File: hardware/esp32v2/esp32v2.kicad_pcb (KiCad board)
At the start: 2 copper layers, 22.5 x 29.8 mm, 10 parts, among them J1 Conn_01x01, J2 Conn_01x02, J3 Conn_01x10, J6 Conn_01x01, U2 ESP32-S3-MINI-1-N8

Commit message: wip
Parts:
- removed C18: 10u, Capacitor_SMD:C_0603_1608Metric
- removed C4: 1u, Capacitor_SMD:C_0603_1608Metric
- removed D2, D4: ESD3.3, Package_TO_SOT_SMD:SOT-723
- removed J1, J6: Conn_01x01, Connector_PinHeader_1.00mm:PinHeader_1x01_P1.00mm_Vertical
- removed R2: 10K, Resistor_SMD:R_0402_1005Metric
- removed U2: ESP32-S3-MINI-1-N8, ESP32_S3_MINI_1_N8:XCVR_ESP32-S3-MINI-1-N8
- added AE1: Antenna, RF_Antenna:Texas_SWRA117D_2.4GHz_Left, F.Cu at (119.0, 32.1)
- added BTN1: BTN, Button_Switch_SMD:SW_Push_1P1T_XKB_TS-1187A, F.Cu at (105.6, 37.5)
- added C1: 12pF, Capacitor_SMD:C_0201_0603Metric, F.Cu at (105.4, 48.7)
- added C10: 0.1uF, Capacitor_SMD:C_0201_0603Metric, F.Cu at (107.9, 44.4)
- added C11: 0.1uF, Capacitor_SMD:C_0201_0603Metric, F.Cu at (119.5, 48.6)
- added C13: 1uF, Capacitor_SMD:C_0201_0603Metric, F.Cu at (116.9, 43.0)
- added C15: 0.1uF, Capacitor_SMD:C_0201_0603Metric, F.Cu at (112.8, 54.0)
- added C19: 0.1uF, Capacitor_SMD:C_0201_0603Metric, F.Cu at (110.2, 53.9)
- added C2: 0.1uF, Capacitor_SMD:C_0201_0603Metric, F.Cu at (107.9, 46.6)
- added C25: 10uF, Capacitor_SMD:C_0201_0603Metric, F.Cu at (107.9, 45.9)
- added C26: 1uF, Capacitor_SMD:C_0201_0603Metric, F.Cu at (107.9, 43.7)
- added C31: 15pF, Capacitor_SMD:C_0201_0603Metric, F.Cu at (119.5, 34.0)
- added C32: 0.1uF, Capacitor_SMD:C_0201_0603Metric, F.Cu at (117.1, 42.2)
- added C33: 12pF, Capacitor_SMD:C_0201_0603Metric, F.Cu at (107.5, 51.2)
- added C37: 12pF, Capacitor_SMD:C_0201_0603Metric, F.Cu at (121.1, 45.4)
- added C38: 12pF, Capacitor_SMD:C_0201_0603Metric, F.Cu at (121.1, 46.1)
- added C39: 1uF, Capacitor_SMD:C_0201_0603Metric, F.Cu at (107.9, 45.2)
- added C40: 10nF, Capacitor_SMD:C_0201_0603Metric, F.Cu at (108.6, 51.2)
- added DNP1: 15pF, Capacitor_SMD:C_0201_0603Metric, F.Cu at (110.3, 53.2)
- added Flash1: Flash, Button_Switch_SMD:SW_Push_1P1T_XKB_TS-1187A, F.Cu at (120.6, 39.0)
- added L3: 2nH, Inductor_SMD:L_0201_0603Metric, F.Cu at (119.7, 49.4)
- added L6: 4.7nH, Inductor_SMD:L_0201_0603Metric, F.Cu at (108.8, 52.7)
- added R21: 10K, Resistor_SMD:R_0201_0603Metric, F.Cu at (113.8, 53.0)
- added R22: 10K, Resistor_SMD:R_0201_0603Metric, F.Cu at (111.8, 54.0)
- added R4: 10K, Resistor_SMD:R_0201_0603Metric, F.Cu at (118.3, 49.0)
- added Reset1: Reset, Button_Switch_SMD:SW_Push_1P1T_XKB_TS-1187A, F.Cu at (102.0, 44.4)
- added U1: ESP32-S3, Package_DFN_QFN:QFN-56-1EP_7x7mm_P0.4mm_EP4x4mm, F.Cu at (113.3, 48.1)
- added U3: W25Q128JVS, Package_SO:SOIC-8_5.3x5.3mm_P1.27mm, F.Cu at (113.4, 38.6)
- added Y1: 32.768 kHz, Crystal:Crystal_SMD_3215-2Pin_3.2x1.5mm, F.Cu at (118.8, 45.9)
- added Y2: 40MHz(10ppm), Crystal:Crystal_SMD_2520-4Pin_2.5x2.0mm, F.Cu at (107.4, 48.7)
- moved J2 1.80 mm to (105.5, 56.5)
- moved J3 0.58 mm to (110.0, 56.8)
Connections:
- J2 pad 2: +3V3 -> VDD_CPU
- J3 pad 1: Net-(J3-Pin_1) -> IO1
- J3 pad 10: /USB_D+ -> USB_D+
- J3 pad 2: Net-(J3-Pin_2) -> IO2
- J3 pad 3: Net-(J3-Pin_3) -> IO3
- J3 pad 4: Net-(J3-Pin_4) -> IO4/BAT
- J3 pad 5: Net-(J3-Pin_5) -> IO5
- J3 pad 6: Net-(J3-Pin_6) -> IO6
- J3 pad 7: Net-(J3-Pin_7) -> IO7
- J3 pad 8: Net-(J3-Pin_8) -> IO8
- J3 pad 9: /USB_D- -> USB_D-
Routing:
- net GND: track 92.1 -> 0.00 mm, vias 38 -> 0
- net +3V3: track 44.3 -> 0.00 mm, vias 2 -> 0
- net /ESP32_EN: track 24.7 -> 0.00 mm
- net Net-(J3-Pin_1): track 14.2 -> 0.00 mm
- net /USB_D+: track 11.4 -> 0.00 mm
- net /USB_D-: track 11.1 -> 0.00 mm
- net Net-(J3-Pin_8): track 11.1 -> 0.00 mm
- net Net-(J3-Pin_7): track 11.0 -> 0.00 mm
- net Net-(J3-Pin_6): track 10.9 -> 0.00 mm
- net Net-(J3-Pin_3): track 10.9 -> 0.00 mm
- net Net-(J3-Pin_5): track 10.9 -> 0.00 mm
- net Net-(J3-Pin_4): track 10.8 -> 0.00 mm
- net Net-(J3-Pin_2): track 10.7 -> 0.00 mm
- net /GPIO0: track 5.24 -> 0.00 mm
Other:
- board size 22.5 x 29.8 mm -> 21 x 29.8 mm

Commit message: wip
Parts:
- removed BTN1: BTN, Button_Switch_SMD:SW_Push_1P1T_XKB_TS-1187A
- removed Flash1: Flash, Button_Switch_SMD:SW_Push_1P1T_XKB_TS-1187A
- removed R4: 10K, Resistor_SMD:R_0201_0603Metric
- removed Reset1: Reset, Button_Switch_SMD:SW_Push_1P1T_XKB_TS-1187A
- removed U3: W25Q128JVS, Package_SO:SOIC-8_5.3x5.3mm_P1.27mm
- added C16: 0.1uF, Capacitor_SMD:C_0201_0603Metric, F.Cu at (115.8, 35.3)
- added J1: Conn_01x02, Connector_JST:JST_SH_BM02B-SRSS-TB_1x02-1MP_P1.00mm_Vertical, F.Cu at (106.0, 50.3)
- added R2: 10K, Resistor_SMD:R_0201_0603Metric, F.Cu at (105.5, 47.0)
- moved C15 19.7 mm to (115.5, 34.5), turned to 45 degrees
- moved C37 18.2 mm to (105.6, 36.0)
- moved DNP1 17.9 mm to (117.3, 36.7), turned to 45 degrees
- moved L6 17.8 mm to (118.0, 37.5), turned to 45 degrees
- moved Y1 16.4 mm to (107.0, 34.5), turned to 180 degrees
- moved C38 15.9 mm to (109.8, 35.0)
- moved C1 15.1 mm to (118.2, 40.8), turned to 45 degrees
- moved C33 13.2 mm to (117.0, 42.0), turned to 45 degrees
- moved C19 12.9 mm to (117.0, 43.0), turned to 45 degrees
- moved J2 12.5 mm to (115.5, 49.0)
- moved C11 11.1 mm to (108.8, 45.3)
- moved C13 10.9 mm to (106.2, 40.7), turned to 135 degrees
- moved C32 10.3 mm to (107.0, 40.5), turned to 135 degrees
- moved C40 8.93 mm to (114.3, 44.2), turned to -135 degrees
- moved R22 8.79 mm to (106.5, 47.0), turned to 90 degrees
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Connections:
- J2 pad 1: GND -> VDD_CPU
- J2 pad 2: VDD_CPU -> GND
- J3 pad 1: IO1 -> USB_D-
- J3 pad 10: USB_D+ -> IO1
- J3 pad 2: IO2 -> USB_D+
- J3 pad 3: IO3 -> IO8
- J3 pad 4: IO4/BAT -> IO7
- J3 pad 5: IO5 -> IO6
- J3 pad 6: IO6 -> IO5
- J3 pad 7: IO7 -> IO4/BAT
- J3 pad 8: IO8 -> IO3
- J3 pad 9: USB_D- -> IO2
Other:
- board size 21 x 29.8 mm -> 18 x 37.5 mm

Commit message: wip
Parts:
- removed C37, C38: 12pF, Capacitor_SMD:C_0201_0603Metric
- removed Y1: 32.768 kHz, Crystal:Crystal_SMD_3215-2Pin_3.2x1.5mm
- moved C32 12.8 mm to (114.8, 50.7), turned to 45 degrees
- moved C13 12.1 mm to (114.0, 50.0), turned to 45 degrees
- moved J1 11.9 mm to (105.2, 38.5), turned to 90 degrees
- moved C31 11.1 mm to (109.2, 38.2), turned to 135 degrees
- moved J2 11.1 mm to (105.0, 52.5)
- moved Y2 10.8 mm to (116.1, 40.6), turned to -45 degrees
- moved C15 9.91 mm to (108.2, 41.2), turned to 135 degrees
- moved C16 8.92 mm to (108.8, 40.8), turned to 135 degrees
- moved C19 8.23 mm to (109.2, 40.2), turned to 135 degrees
- moved L6 7.96 mm to (110.2, 39.2), turned to 135 degrees
- moved J3 7.62 mm to (109.5, 53.8)
- moved DNP1 6.85 mm to (110.7, 38.7), turned to 135 degrees
- moved L3 6.53 mm to (109.7, 39.7), turned to -45 degrees
- moved U1 6.15 mm to (111.4, 45.4), turned to -45 degrees
- moved R22 5.38 mm to (107.7, 41.7), turned to 135 degrees
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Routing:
- net IO1: track 0.00 -> 16.0 mm, vias 0 -> 2
- net IO2: track 0.00 -> 15.1 mm, vias 0 -> 2
- net IO3: track 0.00 -> 14.3 mm, vias 0 -> 2
- net IO4/BAT: track 0.00 -> 13.6 mm, vias 0 -> 2
- net EN: track 0.00 -> 13.4 mm, vias 0 -> 2
- net IO5: track 0.00 -> 13.0 mm, vias 0 -> 2
- net IO6: track 0.00 -> 12.4 mm, vias 0 -> 2
- net IO7: track 0.00 -> 11.8 mm, vias 0 -> 2
- net IO0: track 0.00 -> 11.7 mm
- net IO8: track 0.00 -> 11.2 mm, vias 0 -> 2
- net GND: track 0.00 -> 9.86 mm
- net VDD_CPU: track 0.00 -> 9.32 mm
- net Net-(U1-XTAL_N): track 0.00 -> 6.69 mm
- net USB_D+: track 0.00 -> 5.81 mm
- net USB_D-: track 0.00 -> 5.28 mm
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- removed copper zone on B.Cu, net GND
- removed copper zone on F.Cu, net GND
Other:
- board size 18 x 37.5 mm -> 20 x 25.5 mm
- copper layers 2 -> 4

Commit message: wip esp32 v2
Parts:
- removed AE1: Antenna, RF_Antenna:Texas_SWRA117D_2.4GHz_Left
- moved C32 1.60 mm to (113.2, 51.3)
- moved C13 1.47 mm to (112.7, 50.8)
- moved C16 0.71 mm to (108.3, 40.3)
- moved J1 0.20 mm to (105.2, 38.3)
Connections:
- J3 pad 10: IO1 -> IO38
- J3 pad 3: IO8 -> IO48
- J3 pad 4: IO7 -> IO47
- J3 pad 5: IO6 -> IO33
- J3 pad 6: IO5 -> IO34
- J3 pad 7: IO4/BAT -> IO35
- J3 pad 8: IO3 -> IO36
- J3 pad 9: IO2 -> IO37
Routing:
- net VDD_CPU: track 9.32 -> 25.8 mm, vias 0 -> 6
- net IO1: track 16.0 -> 0.00 mm, vias 2 -> 0
- net IO2: track 15.1 -> 0.00 mm, vias 2 -> 0
- net IO3: track 14.3 -> 0.00 mm, vias 2 -> 0
- net IO4/BAT: track 13.6 -> 0.00 mm, vias 2 -> 0
- net IO5: track 13.0 -> 0.09 mm, vias 2 -> 0
- net IO6: track 12.4 -> 0.00 mm, vias 2 -> 0
- net IO7: track 11.8 -> 0.00 mm, vias 2 -> 0
- net IO8: track 11.2 -> 0.00 mm, vias 2 -> 0
- net GND: track 9.86 -> 20.8 mm, vias 0 -> 9
- net IO38: track 0.00 -> 10.4 mm
- net IO37: track 0.00 -> 8.82 mm
- net IO36: track 0.00 -> 8.24 mm
- net IO35: track 0.00 -> 7.66 mm
- net IO34: track 0.00 -> 7.08 mm
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- added copper zone on B.Cu, net GND
- added copper zone on In1.Cu, net VDD_CPU

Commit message: wip
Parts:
- removed J3: Conn_01x10, LIB_SM10B-SRSS-TB_LF__SN_:SM10B-SRSS-TB
- added J4: Conn_01x02, Connector_Coaxial:U.FL_Molex_MCRF_73412-0110_Vertical, F.Cu at (118.5, 40.5)
- added J5: Conn_01x02, Connector_JST:JST_SH_BM02B-SRSS-TB_1x02-1MP_P1.00mm_Vertical, F.Cu at (105.2, 53.3)
- added S1: Tactile Button, 160gf, PCM_JLCPCB:SW_TS-1088-AR02016, F.Cu at (106.2, 42.5)
- added S2: Tactile Button, 160gf, PCM_JLCPCB:SW_TS-1088-AR02016, F.Cu at (106.3, 39.0)
- C31: value 15pF -> 4pF
- DNP1: value 15pF -> 5pF
- J1: value Conn_01x02 -> Conn_01x08; footprint Connector_JST:JST_SH_BM02B-SRSS-TB_1x02-1MP_P1.00mm_Vertical -> Connector_JST:JST_SHL_SM08B-SHLS-TF_1x08-1MP_P1.00mm_Horizontal
- L6: value 4.7nH -> 1.8nH
- moved J1 23.9 mm to (115.0, 60.0), turned to 0 degrees
- moved C31 10.1 mm to (117.5, 44.0), turned to 0 degrees
- moved Y2 9.30 mm to (119.3, 49.3), turned to -90 degrees
- moved C33 9.27 mm to (119.0, 51.7), turned to 0 degrees
- moved C1 9.13 mm to (119.0, 47.0), turned to 0 degrees
- moved DNP1 8.98 mm to (117.4, 44.7), turned to 0 degrees
- moved C40 7.90 mm to (117.2, 46.4), turned to 90 degrees
- moved L6 7.72 mm to (116.1, 44.2), turned to 90 degrees
- moved L3 7.24 mm to (115.4, 44.2), turned to -90 degrees
- moved C19 6.77 mm to (114.7, 44.2), turned to 90 degrees
- moved J2 6.40 mm to (105.0, 58.9)
- moved C16 6.26 mm to (113.5, 43.7), turned to 180 degrees
- moved C15 6.12 mm to (113.5, 44.4), turned to 180 degrees
- moved R2 5.91 mm to (113.2, 42.3), turned to 0 degrees
- moved R22 5.56 mm to (113.2, 43.0), turned to 180 degrees
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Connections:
- J1 pad 1: IO0 -> IO48
- J1 pad 2: EN -> IO47
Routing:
- net GND: track 20.8 -> 33.4 mm, vias 9 -> 12
- net VDD_CPU: track 25.8 -> 15.9 mm, vias 6 -> 7
- net IO0: track 12.4 -> 7.59 mm, vias 2 -> 0
- net Net-(J4-Pin_1): track 0.77 -> 4.13 mm
- net IO38: track 10.4 -> 7.36 mm
- net IO37: track 8.82 -> 6.45 mm
- net IO36: track 8.24 -> 6.20 mm
- net USB_D-: track 5.28 -> 3.43 mm
- net IO35: track 7.66 -> 5.95 mm
- net USB_D+: track 5.81 -> 4.27 mm
- net IO34: track 7.08 -> 5.70 mm
- net IO33: track 6.50 -> 5.50 mm
- net EN: track 11.1 -> 10.9 mm, vias 2 -> 0
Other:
- board size 20 x 25.5 mm -> 20 x 28 mm

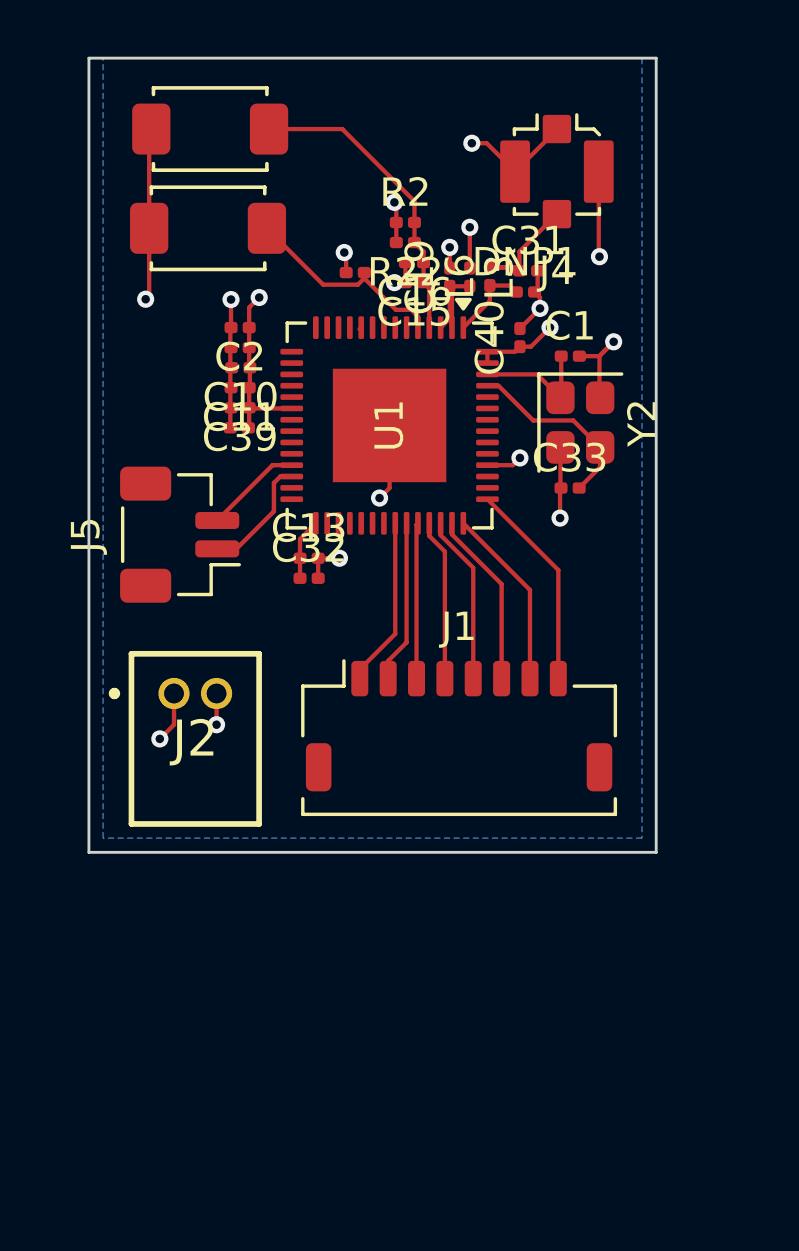
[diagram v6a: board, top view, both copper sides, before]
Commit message: adjust pcb max size
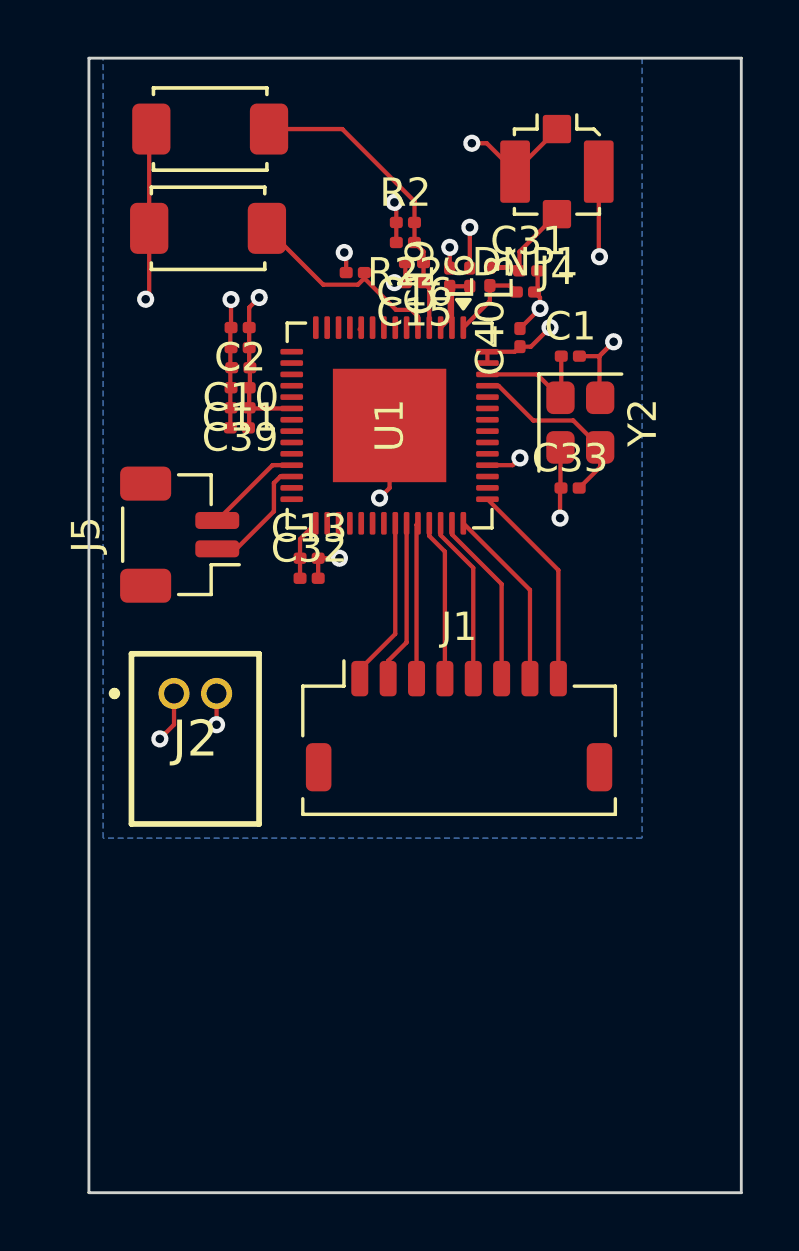
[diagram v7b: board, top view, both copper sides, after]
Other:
- board size 20 x 28 mm -> 23 x 40 mm
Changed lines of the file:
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@@
 	(gr_rect
 		(start 102 36.5)
-		(end 122 64.5)
+		(end 125 76.5)
 		(stroke
 			(width 0.1)
